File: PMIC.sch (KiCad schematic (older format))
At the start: 45 parts, among them J6 USB_B_Micro, J7 Barrel_Jack, SW5 SW_Push, U4 STPMIC1APQR

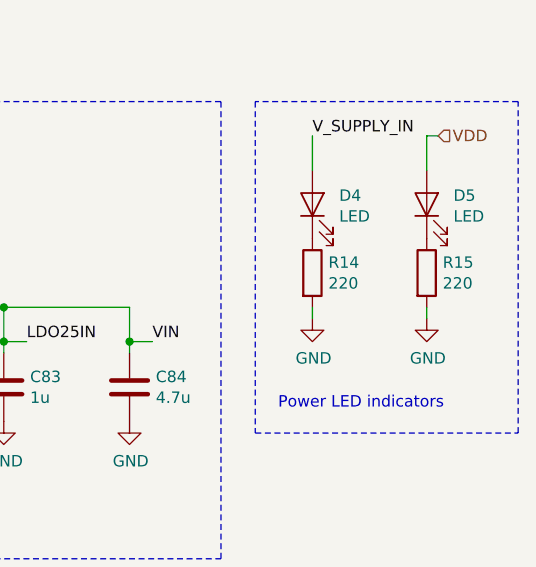
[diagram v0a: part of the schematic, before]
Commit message: Update footprints
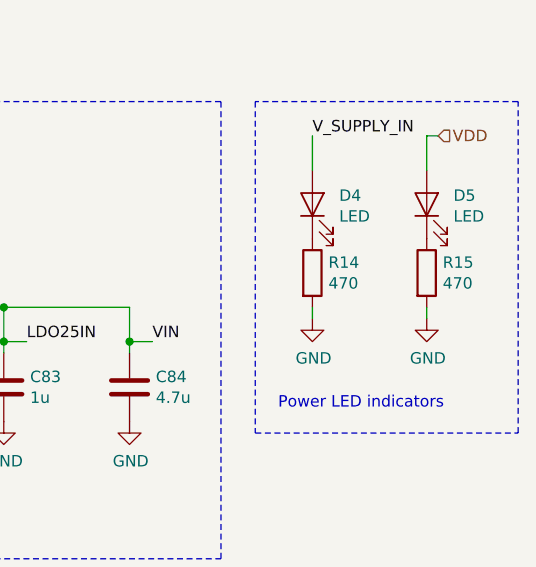
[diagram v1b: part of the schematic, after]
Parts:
- C68, C69, C70, C71, C72, C73, C74, C75, C76, C80, C82, C83, C84: footprint (none) -> Capacitor_SMD:C_0603_1608Metric
- R14, R15: value 220 -> 470; footprint Resistor_SMD:R_0603_1608Metric -> Resistor_SMD:R_0603_1608Metric_Pad1.05x0.95mm_HandSolder
- R34, R35: footprint (none) -> Resistor_SMD:R_0603_1608Metric_Pad1.05x0.95mm_HandSolder
- SW5: footprint (none) -> Button_Switch_SMD:SW_Push_1P1T_NO_6x6mm_H9.5mm
- TP1: footprint (none) -> TestPoint:TestPoint_Pad_D2.0mm
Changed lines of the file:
@@
 P 9850 5150
 F 0 "R14" H 9920 5196 50  0000 L CNN
-F 1 "220" H 9920 5105 50  0000 L CNN
-F 2 "Resistor_SMD:R_0603_1608Metric" V 9780 5150 50  0001 C CNN
+F 1 "470" H 9920 5105 50  0000 L CNN
+F 2 "Resistor_SMD:R_0603_1608Metric_Pad1.05x0.95mm_HandSolder" V 9780 5150 50  0001 C CNN
 F 3 "~" H 9850 5150 50  0001 C CNN
 	1    9850 5150
@@
 P 10350 5150
 F 0 "R15" H 10420 5196 50  0000 L CNN
-F 1 "220" H 10420 5105 50  0000 L CNN
-F 2 "Resistor_SMD:R_0603_1608Metric" V 10280 5150 50  0001 C CNN
+F 1 "470" H 10420 5105 50  0000 L CNN
+F 2 "Resistor_SMD:R_0603_1608Metric_Pad1.05x0.95mm_HandSolder" V 10280 5150 50  0001 C CNN
 F 3 "~" H 10350 5150 50  0001 C CNN
 	1    10350 5150
@@
 F 0 "C71" H 1865 5546 50  0000 L CNN
 F 1 "4.7u" H 1865 5455 50  0000 L CNN
-F 2 "" H 1788 5350 50  0001 C CNN
+F 2 "Capacitor_SMD:C_0603_1608Metric" H 1788 5350 50  0001 C CNN
 F 3 "~" H 1750 5500 50  0001 C CNN
 	1    1750 5500
@@
 F 0 "C68" H 1815 6196 50  0000 L CNN
 F 1 "4.7u" H 1815 6105 50  0000 L CNN
-F 2 "" H 1738 6000 50  0001 C CNN
+F 2 "Capacitor_SMD:C_0603_1608Metric" H 1738 6000 50  0001 C CNN
 F 3 "~" H 1700 6150 50  0001 C CNN
 	1    1700 6150
@@
 F 0 "C74" H 3015 6196 50  0000 L CNN
 F 1 "4.7u" H 3015 6105 50  0000 L CNN
-F 2 "" H 2938 6000 50  0001 C CNN
+F 2 "Capacitor_SMD:C_0603_1608Metric" H 2938 6000 50  0001 C CNN
 F 3 "~" H 2900 6150 50  0001 C CNN
 	1    2900 6150
@@
 F 0 "C69" H 1815 6846 50  0000 L CNN
 F 1 "4.7u" H 1815 6755 50  0000 L CNN
-F 2 "" H 1738 6650 50  0001 C CNN
+F 2 "Capacitor_SMD:C_0603_1608Metric" H 1738 6650 50  0001 C CNN
 F 3 "~" H 1700 6800 50  0001 C CNN
 	1    1700 6800
@@
 F 0 "C75" H 3015 6846 50  0000 L CNN
 F 1 "220u" H 3015 6755 50  0000 L CNN
-F 2 "" H 2938 6650 50  0001 C CNN
+F 2 "Capacitor_SMD:C_0603_1608Metric" H 2938 6650 50  0001 C CNN
 F 3 "~" H 2900 6800 50  0001 C CNN
 	1    2900 6800
@@
 F 0 "C70" H 1865 4846 50  0000 L CNN
 F 1 "1u" H 1865 4755 50  0000 L CNN
-F 2 "" H 1788 4650 50  0001 C CNN
+F 2 "Capacitor_SMD:C_0603_1608Metric" H 1788 4650 50  0001 C CNN
 F 3 "~" H 1750 4800 50  0001 C CNN
 	1    1750 4800
@@
 F 0 "C82" H 8065 5696 50  0000 L CNN
 F 1 "1u" H 8065 5605 50  0000 L CNN
-F 2 "" H 7988 5500 50  0001 C CNN
+F 2 "Capacitor_SMD:C_0603_1608Metric" H 7988 5500 50  0001 C CNN
 F 3 "~" H 7950 5650 50  0001 C CNN
 	1    7950 5650
@@
 F 0 "C83" H 8615 5696 50  0000 L CNN
 F 1 "1u" H 8615 5605 50  0000 L CNN
-F 2 "" H 8538 5500 50  0001 C CNN
+F 2 "Capacitor_SMD:C_0603_1608Metric" H 8538 5500 50  0001 C CNN
 F 3 "~" H 8500 5650 50  0001 C CNN
 	1    8500 5650
@@
 F 0 "C72" H 3015 4846 50  0000 L CNN
 F 1 "10u" H 3015 4755 50  0000 L CNN
-F 2 "" H 2938 4650 50  0001 C CNN
+F 2 "Capacitor_SMD:C_0603_1608Metric" H 2938 4650 50  0001 C CNN
 F 3 "~" H 2900 4800 50  0001 C CNN
 	1    2900 4800
@@
 F 0 "C80" H 7315 4796 50  0000 L CNN
 F 1 "10u" H 7315 4705 50  0000 L CNN
-F 2 "" H 7238 4600 50  0001 C CNN
+F 2 "Capacitor_SMD:C_0603_1608Metric" H 7238 4600 50  0001 C CNN
 F 3 "~" H 7200 4750 50  0001 C CNN
 	1    7200 4750
@@
 F 0 "C84" H 9165 5696 50  0000 L CNN
 F 1 "4.7u" H 9165 5605 50  0000 L CNN
-F 2 "" H 9088 5500 50  0001 C CNN
+F 2 "Capacitor_SMD:C_0603_1608Metric" H 9088 5500 50  0001 C CNN
 F 3 "~" H 9050 5650 50  0001 C CNN
 	1    9050 5650
@@
 F 0 "R34" V 2943 6600 50  0000 C CNN
 F 1 "0" V 3034 6600 50  0000 C CNN
-F 2 "" V 3080 6600 50  0001 C CNN
+F 2 "Resistor_SMD:R_0603_1608Metric_Pad1.05x0.95mm_HandSolder" V 3080 6600 50  0001 C CNN
 F 3 "~" H 3150 6600 50  0001 C CNN
 	1    3150 6600
@@
 F 0 "C73" H 3015 5546 50  0000 L CNN
 F 1 "4.7u" H 3015 5455 50  0000 L CNN
-F 2 "" H 2938 5350 50  0001 C CNN
+F 2 "Capacitor_SMD:C_0603_1608Metric" H 2938 5350 50  0001 C CNN
 F 3 "~" H 2900 5500 50  0001 C CNN
 	1    2900 5500
@@
 F 0 "C76" H 4215 6196 50  0000 L CNN
 F 1 "4.7u" H 4215 6105 50  0000 L CNN
-F 2 "" H 4138 6000 50  0001 C CNN
+F 2 "Capacitor_SMD:C_0603_1608Metric" H 4138 6000 50  0001 C CNN
 F 3 "~" H 4100 6150 50  0001 C CNN
 	1    4100 6150
@@
 F 0 "SW5" V 7604 3648 50  0000 L CNN
 F 1 "SW_Push" V 7695 3648 50  0000 L CNN
-F 2 "" H 7650 3700 50  0001 C CNN
+F 2 "Button_Switch_SMD:SW_Push_1P1T_NO_6x6mm_H9.5mm" H 7650 3700 50  0001 C CNN
 F 3 "~" H 7650 3700 50  0001 C CNN
 	1    7650 3500
@@
 F 0 "TP1" H 8008 5418 50  0000 L CNN
 F 1 "TestPoint" H 8008 5327 50  0000 L CNN
-F 2 "" H 8150 5300 50  0001 C CNN
+F 2 "TestPoint:TestPoint_Pad_D2.0mm" H 8150 5300 50  0001 C CNN
 F 3 "~" H 8150 5300 50  0001 C CNN
 	1    7950 5300
@@
 F 0 "R35" V 8250 1700 50  0000 C CNN
 F 1 "0" V 8250 1600 50  0000 C CNN
-F 2 "" V 8080 1650 50  0001 C CNN
+F 2 "Resistor_SMD:R_0603_1608Metric_Pad1.05x0.95mm_HandSolder" V 8080 1650 50  0001 C CNN
 F 3 "~" H 8150 1650 50  0001 C CNN
 	1    8150 1650

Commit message: Update jtag connector to swd
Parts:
- J7: footprint (none) -> Connector_BarrelJack:BarrelJack_Wuerth_6941xx301002
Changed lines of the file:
@@
 $EndDescr
-$Comp
-L LinuxBoard:STPMIC1APQR U4
-U 1 1 60173C27
-P 2950 1400
-F 0 "U4" H 3950 1787 60  0000 C CNN
-F 1 "STPMIC1APQR" H 3950 1681 60  0000 C CNN
-F 2 "LinuxBoard:STPMIC1APQR" H 3950 1640 60  0001 C CNN
-F 3 "" H 2950 1400 60  0000 C CNN
-	1    2950 1400
-	1    0    0    -1
-$EndComp
 $Comp
 L Connector:USB_B_Micro J?
@@
 F 0 "J7" H 7400 2700 50  0000 C CNN
 F 1 "Barrel_Jack" H 7400 2600 50  0000 C CNN
-F 2 "" H 7500 2310 50  0001 C CNN
+F 2 "Connector_BarrelJack:BarrelJack_Wuerth_6941xx301002" H 7500 2310 50  0001 C CNN
 F 3 "~" H 7500 2310 50  0001 C CNN
 	1    7450 2350
@@
 Wire Wire Line
 	3350 6600 3450 6600
+$Comp
+L LinuxBoard:STPMIC1APQR U4
+U 1 1 60173C27
+P 2950 1400
+F 0 "U4" H 3950 1787 60  0000 C CNN
+F 1 "STPMIC1APQR" H 3950 1681 60  0000 C CNN
+F 2 "LinuxBoard:STPMIC1APQR" H 3950 1640 60  0001 C CNN
+F 3 "" H 2950 1400 60  0000 C CNN
+	1    2950 1400
+	1    0    0    -1
+$EndComp
 $EndSCHEMATC

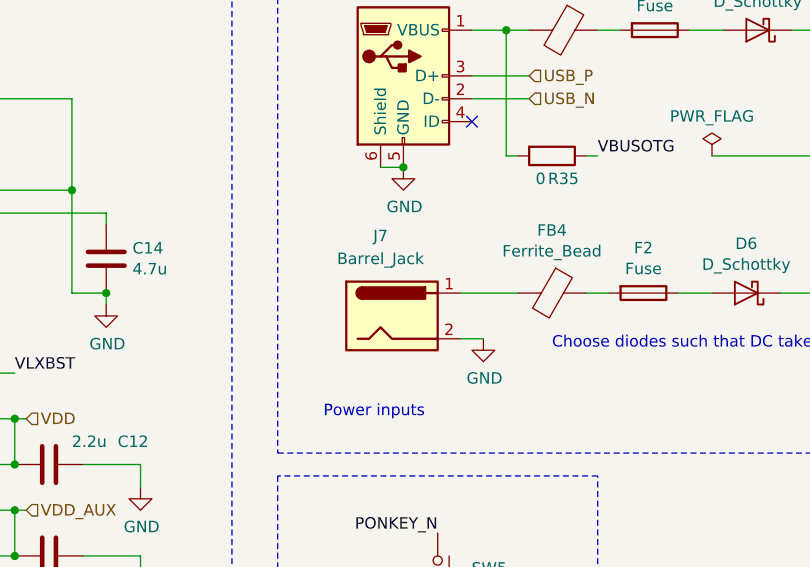
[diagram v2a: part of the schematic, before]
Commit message: Fix footprints
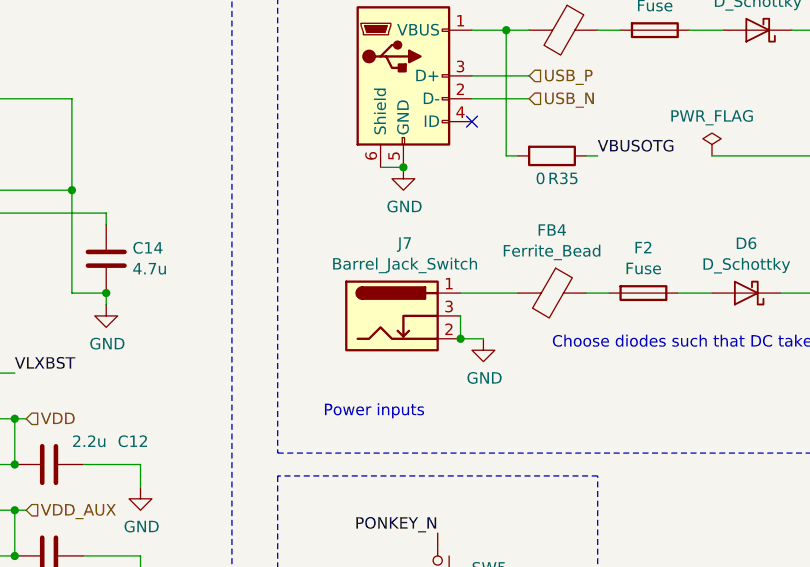
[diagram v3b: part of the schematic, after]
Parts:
- removed J7: Barrel_Jack, Connector_BarrelJack:BarrelJack_Wuerth_6941xx301002, symbol Connector:Barrel_Jack
- added J7: Barrel_Jack_Switch, Connector_BarrelJack:BarrelJack_Wuerth_6941xx301002, symbol Connector:Barrel_Jack_Switch
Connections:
- net GND: now also J7.2, J7.3
- net at FB4.2: now also J7.1
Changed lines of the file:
@@
 USB_N
-$Comp
-L Connector:Barrel_Jack J7
-U 1 1 61B3572E
-P 7450 2350
-F 0 "J7" H 7400 2700 50  0000 C CNN
-F 1 "Barrel_Jack" H 7400 2600 50  0000 C CNN
-F 2 "Connector_BarrelJack:BarrelJack_Wuerth_6941xx301002" H 7500 2310 50  0001 C CNN
-F 3 "~" H 7500 2310 50  0001 C CNN
-	1    7450 2350
-	1    0    0    -1
-$EndComp
 $Comp
 L power:PWR_FLAG #FLG?
@@
 	1    0    0    -1
 $EndComp
+$Comp
+L Connector:Barrel_Jack_Switch J7
+U 1 1 609E9DC9
+P 7450 2350
+F 0 "J7" H 7507 2667 50  0000 C CNN
+F 1 "Barrel_Jack_Switch" H 7507 2576 50  0000 C CNN
+F 2 "Connector_BarrelJack:BarrelJack_Wuerth_6941xx301002" H 7500 2310 50  0001 C CNN
+F 3 "~" H 7500 2310 50  0001 C CNN
+	1    7450 2350
+	1    0    0    -1
+$EndComp
+Wire Wire Line
+	7750 2450 7750 2350
+Connection ~ 7750 2450
 $EndSCHEMATC

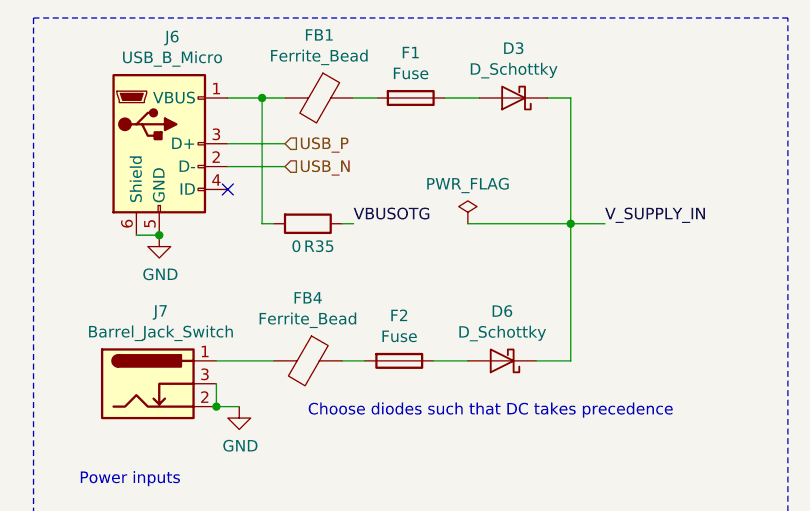
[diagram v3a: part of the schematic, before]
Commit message: Add mounting holes
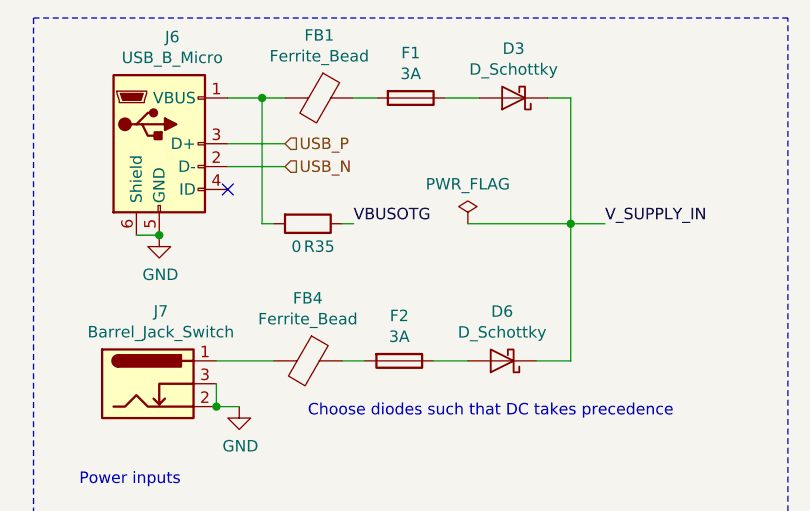
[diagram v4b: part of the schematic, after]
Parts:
- F1, F2: value Fuse -> 3A
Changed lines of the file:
@@
 AR Path="/60172B24/60637B91" Ref="F1"  Part="1"
 F 0 "F1" V 8403 1100 50  0000 C CNN
-F 1 "Fuse" V 8494 1100 50  0000 C CNN
+F 1 "3A" V 8494 1100 50  0000 C CNN
 F 2 "Fuse:Fuse_0603_1608Metric" V 8530 1100 50  0001 C CNN
 F 3 "~" H 8600 1100 50  0001 C CNN
@@
 AR Path="/60172B24/61B46629" Ref="F2"  Part="1"
 F 0 "F2" V 8353 2250 50  0000 C CNN
-F 1 "Fuse" V 8444 2250 50  0000 C CNN
+F 1 "3A" V 8444 2250 50  0000 C CNN
 F 2 "Fuse:Fuse_0603_1608Metric" V 8480 2250 50  0001 C CNN
 F 3 "~" H 8550 2250 50  0001 C CNN

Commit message: Schematic signoff
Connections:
- net USB_N renamed USB2_N
- net USB_P renamed USB2_P
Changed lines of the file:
@@
 $Descr A4 11693 8268
 encoding utf-8
-Sheet 5 6
+Sheet 4 6
 Title ""
 Date ""
@@
 	1100 750  1100 4150
 Text HLabel 8050 1300 2    50   Input ~ 0
-USB_P
+USB2_P
 Text HLabel 8050 1400 2    50   Input ~ 0
-USB_N
+USB2_N
 $Comp
 L power:PWR_FLAG #FLG?
